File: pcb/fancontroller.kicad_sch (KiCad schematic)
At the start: 6 parts, among them J1 Thermo

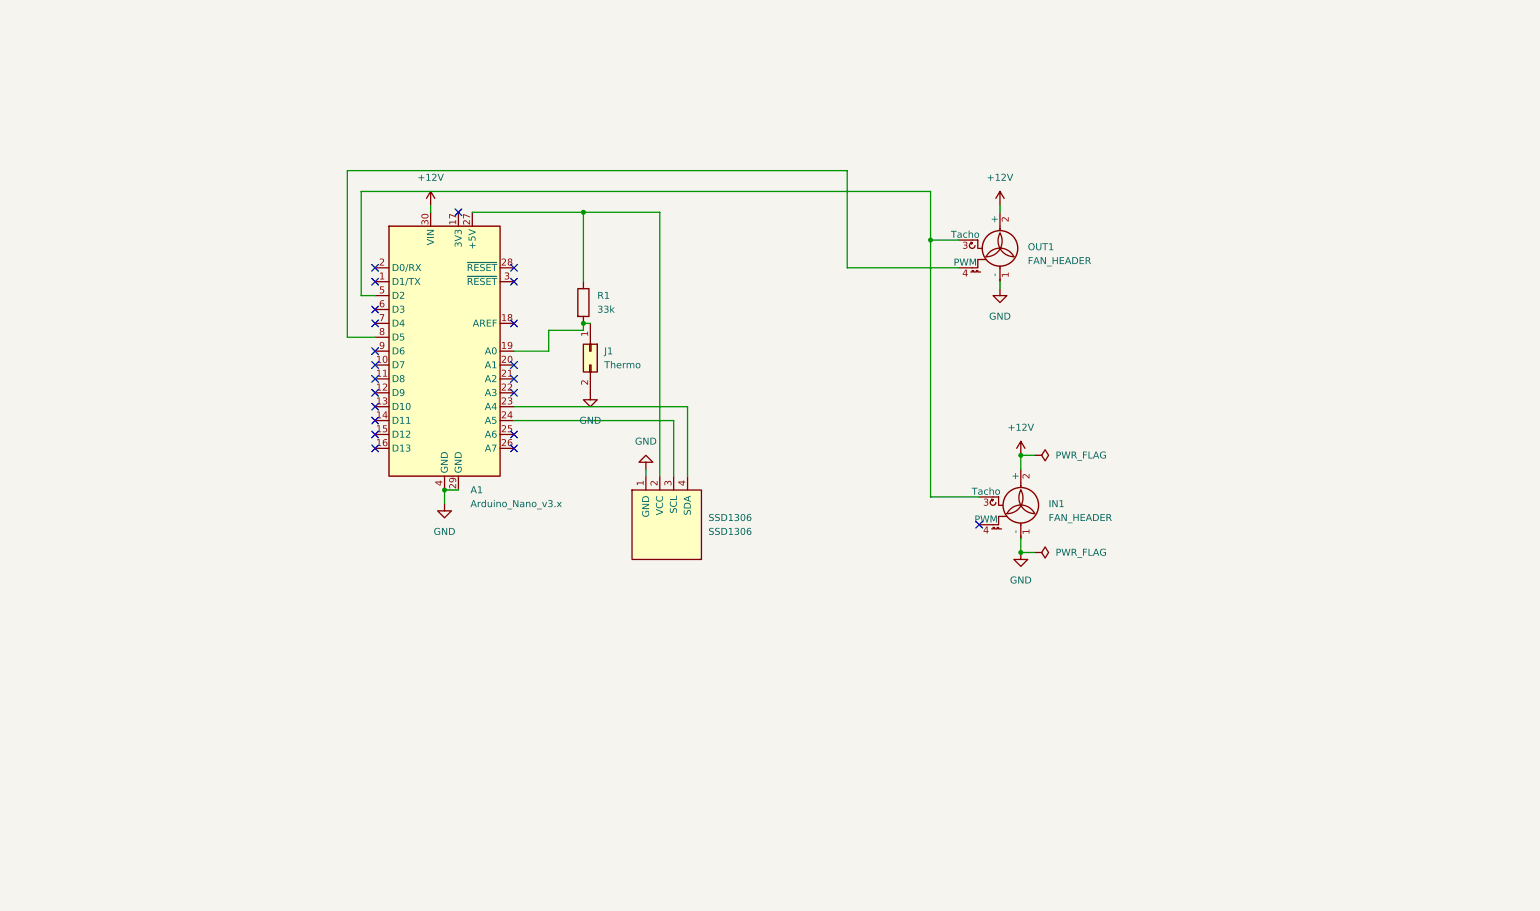
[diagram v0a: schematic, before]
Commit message: Update to Kicad 8, clean up schematic, add second fan header to schematic
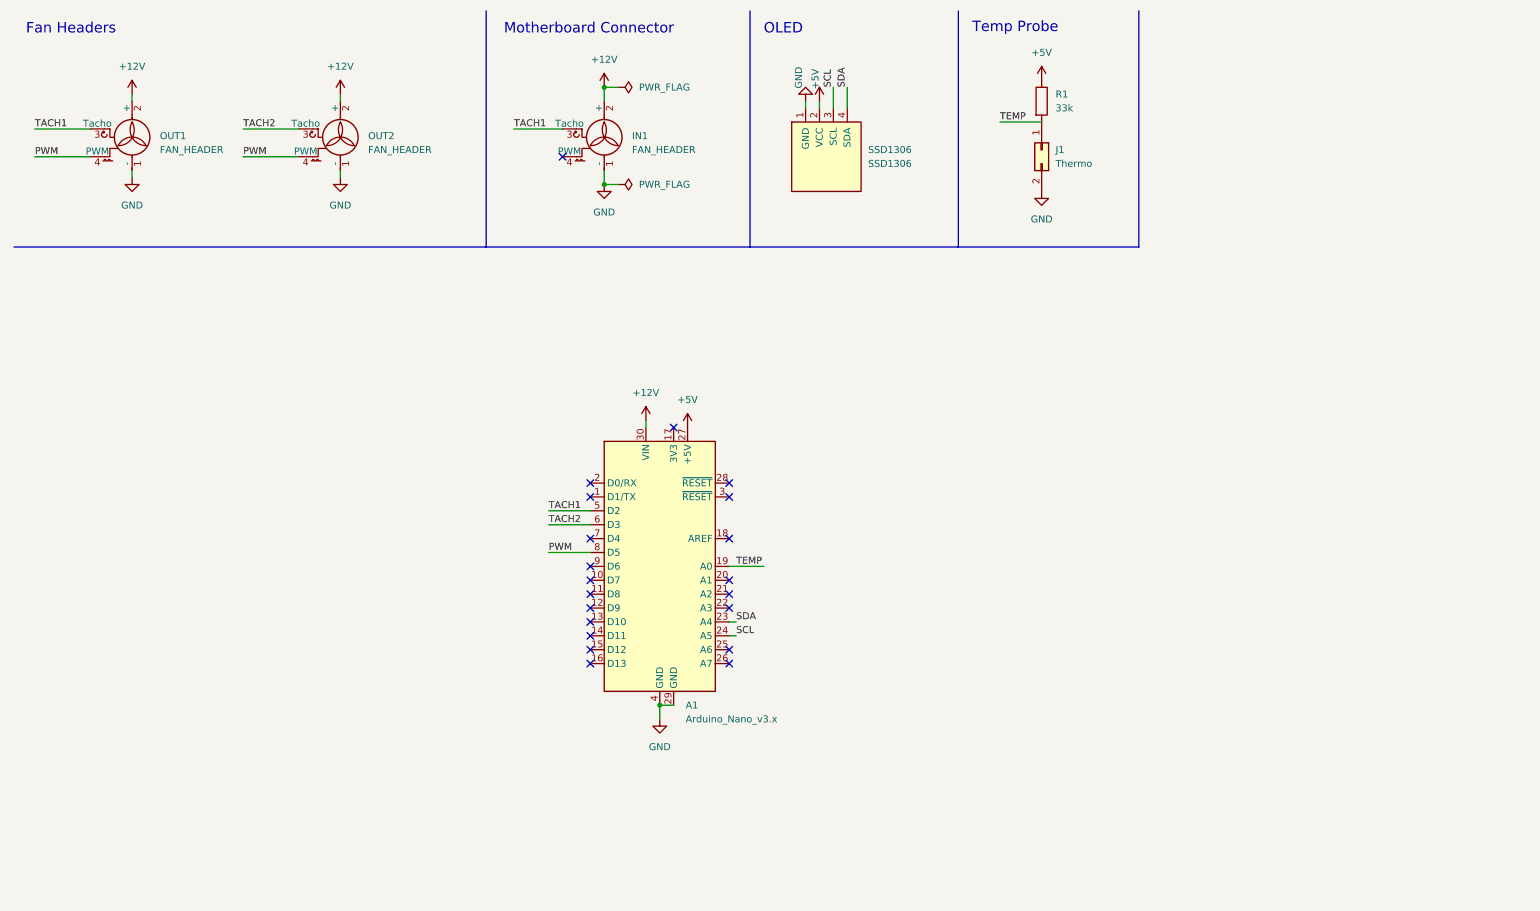
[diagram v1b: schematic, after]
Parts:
- added OUT2: FAN_HEADER, Connector:FanPinHeader_1x04_P2.54mm_Vertical, symbol Motor:Fan_CPU_4pin
- SSD1306: symbol SSD1306:SSD1306 -> SSD1306-128x64_OLED:SSD1306
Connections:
- net +12V: now also OUT2.2 (+)
- net GND: now also OUT2.1 (-)
- net TEMP: now reaches A1.19 (A0), J1.1 (Pin_1), R1.2
- net SDA: now reaches A1.23 (A4), SSD1306.4 (SDA)
- net SCL: now reaches A1.24 (A5), SSD1306.3 (SCL)
- net +5V: now reaches A1.27 (+5V), R1.1, SSD1306.2 (VCC)
- net TACH1: now reaches A1.5 (D2), IN1.3 (Tacho), OUT1.3 (Tacho)
- net TACH2: now reaches A1.6 (D3)
- net TACH2: now also OUT2.3 (Tacho)
- net PWM: now reaches A1.8 (D5), OUT1.4 (PWM)
- net PWM: now also OUT2.4 (PWM)
- no-connect marks 22 -> 21
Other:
- note added: "Fan Headers"
- note added: "Motherboard Connector"
- note added: "OLED"
- note added: "Temp Probe"
- company: (none) -> @funrollloops
- title: (none) -> Fan Controller
- moved on the sheet: A1, IN1, J1, OUT1, R1, SSD1306

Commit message: wip: switch to stm32f103
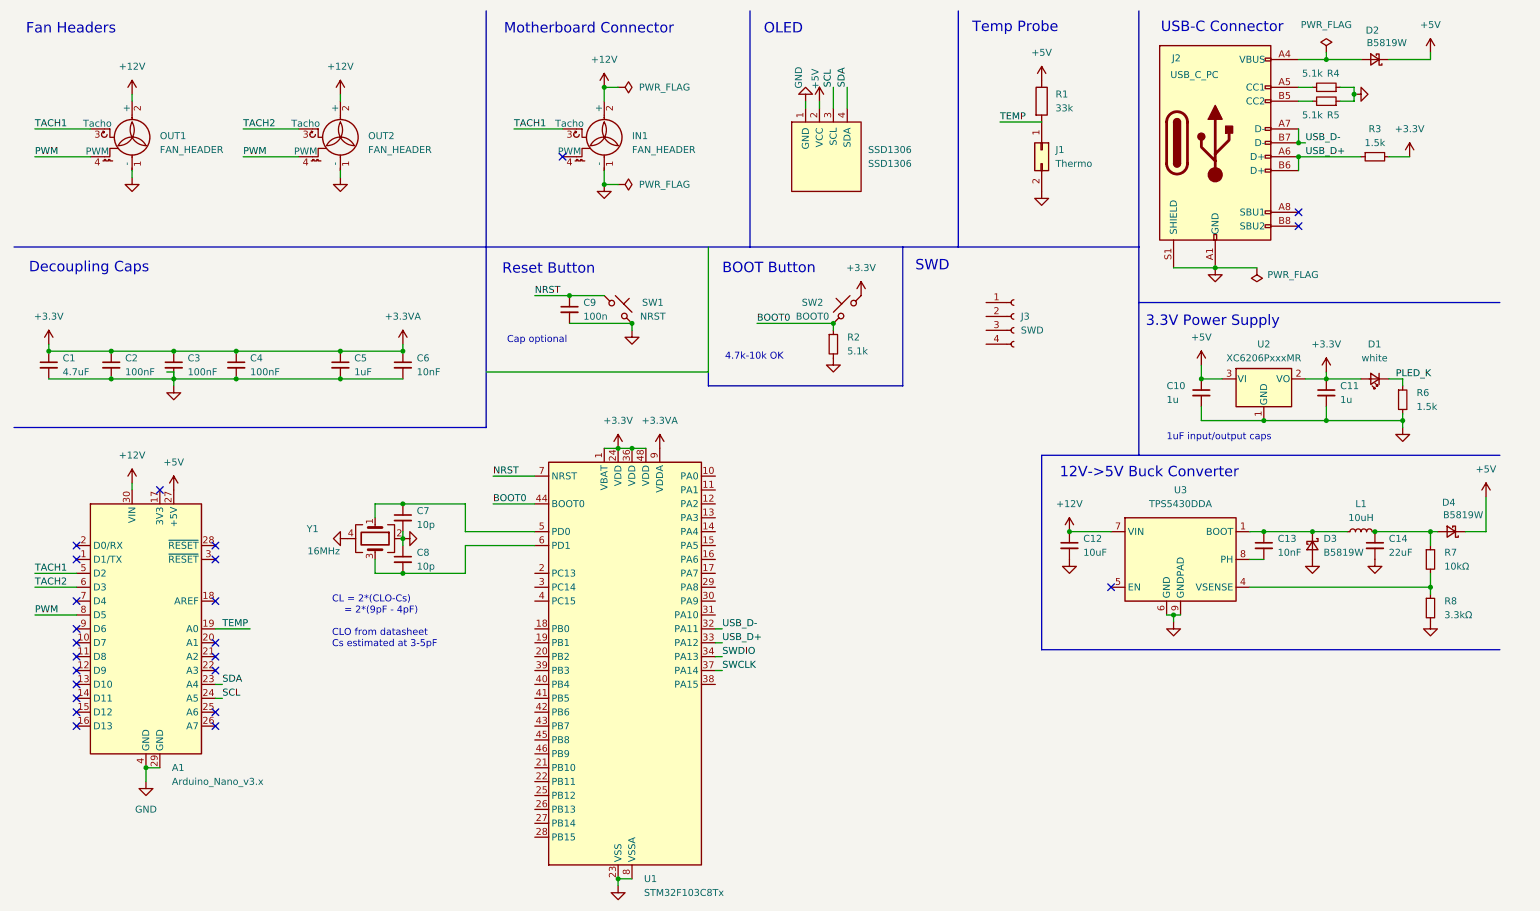
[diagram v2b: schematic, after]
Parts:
- added C1: 4.7uF, symbol Device:C_Small
- added C10, C11: 1u, Capacitor_SMD:C_0402_1005Metric, symbol Device:C_Small
- added C12: 10uF, symbol Device:C_Small
- added C13, C6: 10nF, symbol Device:C_Small
- added C14: 22uF, symbol Device:C_Small
- added C2, C3, C4: 100nF, symbol Device:C_Small
- added C5: 1uF, symbol Device:C_Small
- added C7, C8: 10p, Capacitor_SMD:C_0402_1005Metric, symbol Device:C_Small
- added C9: 100n, Capacitor_SMD:C_0402_1005Metric, symbol Device:C_Small
- added D1: white, LED_SMD:LED_0603_1608Metric, symbol Device:LED_Small
- added D2, D3, D4: B5819W, Diode_SMD:D_SOD-123, symbol Device:D_Schottky_Small
- added J2: USB_C_PC, Connector_USB:USB_C_Receptacle_XKB_U262-16XN-4BVC11, symbol Connector:USB_C_Receptacle_USB2.0_16P
- added J3: SWD, Connector_PinSocket_2.54mm:PinSocket_1x04_P2.54mm_Vertical, symbol Connector:Conn_01x04_Socket
- added L1: 10uH, symbol Device:L_Small
- added R2, R4, R5: 5.1k, Resistor_SMD:R_0402_1005Metric, symbol Device:R_Small
- added R3, R6: 1.5k, Resistor_SMD:R_0402_1005Metric, symbol Device:R_Small
- added R7: 10kΩ, symbol Device:R_Small
- added R8: 3.3kΩ, symbol Device:R_Small
- added SW1: NRST, Button_Switch_SMD:SW_Push_1P1T_XKB_TS-1187A, symbol Switch:SW_Push_45deg
- added SW2: BOOT0, Button_Switch_SMD:SW_Push_1P1T_XKB_TS-1187A, symbol Switch:SW_Push_45deg
- added U1: STM32F103C8Tx, Package_QFP:LQFP-48_7x7mm_P0.5mm, symbol MCU_ST_STM32F1:STM32F103C8Tx
- added U2: XC6206PxxxMR, Package_TO_SOT_SMD:SOT-23-3, symbol Regulator_Linear:XC6206PxxxMR
- added U3: TPS5430DDA, Package_SO:TI_SO-PowerPAD-8_ThermalVias, symbol Regulator_Switching:TPS5430DDA
- added Y1: 16MHz, Crystal:Crystal_SMD_3225-4Pin_3.2x2.5mm, symbol Device:Crystal_GND24
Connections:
- net +12V: now also C12.1, U3.7 (VIN)
- net +5V: now also C10.1, D2.1 (K), D4.1 (K), U2.3 (VI)
- net GND: now also C1.2, C10.2, C11.2, C12.2, C14.2, C2.2, C3.2, C4.2, C5.2, C6.2, C7.2, C8.1, C9.2, D3.2 (A), J2.A1 (GND), J2.A12 (GND), J2.B1 (GND), J2.B12 (GND), J2.S1 (SHIELD), R2.2, R4.1, R5.1, R6.2, R8.2, SW1.2, U1.23 (VSS), U1.35 (VSS), U1.47 (VSS), U1.8 (VSSA), U2.1 (GND), U3.6 (GND), U3.9 (GNDPAD), Y1.2, Y1.4
- new net: C13.1, D3.1 (K), L1.1, U3.1 (BOOT)
- new net: C13.2, U3.8 (PH)
- new net: D2.2 (A), J2.A4 (VBUS), J2.A9 (VBUS), J2.B4 (VBUS), J2.B9 (VBUS)
- new net: J2.A5 (CC1), R4.2
- new net: J2.B5 (CC2), R5.2
- new net: C14.1, D4.2 (A), L1.2, R7.1
- new net: C7.1, U1.5 (PD0), Y1.1
- new net: C8.2, U1.6 (PD1), Y1.3
- new net: R7.2, R8.1, U3.4 (VSENSE)
- new net +3.3V: C1.1, C11.1, C2.1, C3.1, C4.1, C5.1, C6.1, D1.2 (A), R3.2, SW2.1, U1.1 (VBAT), U1.24 (VDD), U1.36 (VDD), U1.48 (VDD), U1.9 (VDDA), U2.2 (VO)
- new net BOOT0: R2.1, SW2.2, U1.44 (BOOT0)
- new net NRST: C9.1, SW1.1, U1.7 (NRST)
- new net PLED_K: D1.1 (K), R6.1
- new net SWCLK: U1.37 (PA14)
- new net SWDIO: U1.34 (PA13)
- new net USB_D+: J2.A6 (D+), J2.B6 (D+), R3.1, U1.33 (PA12)
- new net USB_D-: J2.A7 (D-), J2.B7 (D-), U1.32 (PA11)
- no-connect marks 21 -> 24
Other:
- note added: "12V->5V Buck Converter"
- note added: "1uF input/output caps"
- note added: "3.3V Power Supply"
- note added: "4.7k-10k OK"
- note added: "BOOT Button"
- note added: "CL = 2*(CLO-Cs) = 2*(9pF - 4pF) CLO from datasheet Cs estimated at 3-5pF"
- note added: "Cap optional"
- note added: "Decoupling Caps"
- note added: "Reset Button"
- note added: "SWD"
- note added: "USB-C Connector"
- moved on the sheet: A1

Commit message: v2: add stm32cubemx config, early draft of pcb layout, update version
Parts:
- removed A1: Arduino_Nano_v3.x, Module:Arduino_Nano, symbol MCU_Module:Arduino_Nano_v3.x
- added U4: USBLC6-2SC6, Package_TO_SOT_SMD:SOT-23-6, symbol Power_Protection:USBLC6-2SC6
- C1, C13, C2, C3, C4, C5, C6: footprint (none) -> Capacitor_SMD:C_0402_1005Metric
- C10, C11: value 1u -> 1uF
- C12, C14: footprint (none) -> Capacitor_SMD:C_0603_1608Metric
- C7, C8: value 10p -> 10pF
- L1: footprint (none) -> Inductor_SMD:L_1210_3225Metric
- R1: value 33k -> 33kΩ; footprint Resistor_THT:R_Axial_DIN0207_L6.3mm_D2.5mm_P7.62mm_Horizontal -> Resistor_SMD:R_0402_1005Metric
- R2, R4, R5: value 5.1k -> 5.1kΩ
- R3, R6: value 1.5k -> 1.5kΩ
- R7, R8: footprint (none) -> Resistor_SMD:R_0402_1005Metric
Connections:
- net +3.3V: now also J3.4 (Pin_4), R1.1, SSD1306.2 (VCC)
- net +5V: no longer R1.1, SSD1306.2 (VCC)
- net GND: now also J3.1 (Pin_1), U4.2 (GND)
- net PWM: now also U1.28 (PB15)
- net SCL: now also U1.42 (PB6)
- net SDA: now also U1.43 (PB7)
- net SWCLK: now also J3.2 (Pin_2)
- net SWDIO: now also J3.3 (Pin_3)
- net TACH1: now also U1.25 (PB12)
- net TACH2: now also U1.26 (PB13)
- net TEMP: now also U1.11 (PA1)
- net USB_D+: now also U4.1 (I/O1), U4.6 (I/O1)
- net USB_D-: now also U4.3 (I/O2), U4.4 (I/O2)
- net at C13.1, U3.1 (BOOT): no longer D3.1 (K), L1.1
- net at C13.2, U3.8 (PH): now also D3.1 (K), L1.1
- net VBUS: now reaches D2.2 (A), J2.A4 (VBUS), J2.A9 (VBUS), J2.B4 (VBUS), J2.B9 (VBUS)
- net VBUS: now also U4.5 (VBUS)
- no-connect marks 24 -> 29
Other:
- note added: "5V -> 3.3V LDO"
- note removed: "3.3V Power Supply"
- title: Fan Controller -> Fan Controller (v2, WIP)
- moved on the sheet: D2, J3, L1, R3

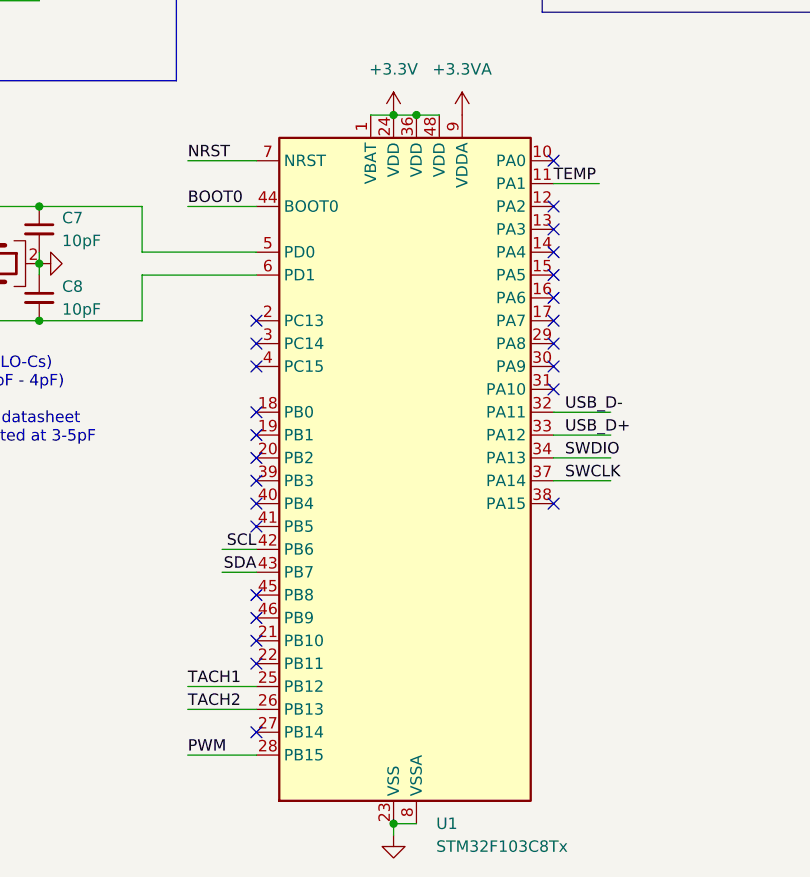
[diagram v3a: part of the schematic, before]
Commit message: Finish routing assuming OLED module
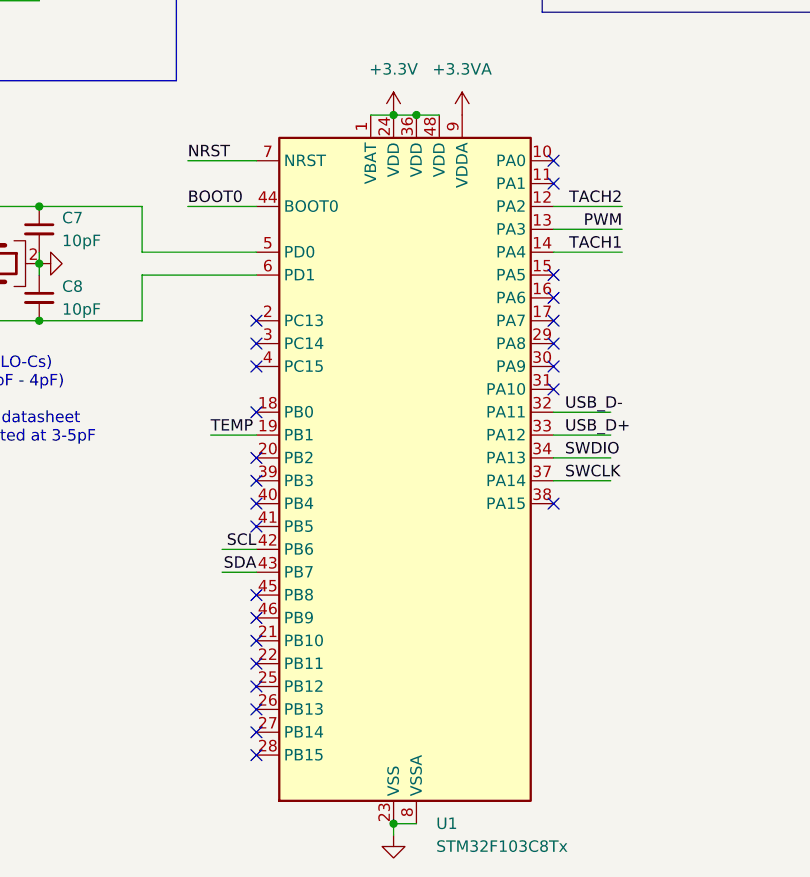
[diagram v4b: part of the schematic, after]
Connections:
- net PWM: now also U1.13 (PA3); no longer U1.28 (PB15)
- net TACH1: now also U1.14 (PA4); no longer U1.25 (PB12)
- net TACH2: now also U1.12 (PA2); no longer U1.26 (PB13)
- net TEMP: now also U1.19 (PB1); no longer U1.11 (PA1)
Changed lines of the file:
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@@
+	)
+	(no_connect
+		(at 107.95 158.75)
+	)
+	(no_connect
+		(at 107.95 156.21)
 	)
 	(no_connect
@@
 	)
 	(no_connect
-		(at 140.97 102.87)
-	)
-	(no_connect
 		(at 107.95 125.73)
 	)
@@
 	)
 	(no_connect
+		(at 107.95 163.83)
+	)
+	(no_connect
 		(at 107.95 133.35)
 	)
@@
 	)
 	(no_connect
-		(at 140.97 107.95)
+		(at 140.97 100.33)
 	)
 	(no_connect
@@
 	)
 	(no_connect
-		(at 140.97 105.41)
-	)
-	(no_connect
 		(at 140.97 97.79)
 	)
@@
 	)
 	(no_connect
-		(at 107.95 128.27)
-	)
-	(no_connect
 		(at 140.97 118.11)
 	)
@@
 	(wire
 		(pts
-			(xy 100.33 158.75) (xy 107.95 158.75)
+			(xy 148.59 102.87) (xy 140.97 102.87)
 		)
 		(stroke
@@
 	(wire
 		(pts
-			(xy 140.97 100.33) (xy 146.05 100.33)
+			(xy 102.87 128.27) (xy 107.95 128.27)
 		)
 		(stroke
@@
 	(wire
 		(pts
-			(xy 100.33 156.21) (xy 107.95 156.21)
+			(xy 148.59 107.95) (xy 140.97 107.95)
 		)
 		(stroke
@@
 	(wire
 		(pts
-			(xy 100.33 163.83) (xy 107.95 163.83)
+			(xy 148.59 105.41) (xy 140.97 105.41)
 		)
 		(stroke
@@
 	)
 	(label "TACH1"
-		(at 100.33 156.21 0)
-		(fields_autoplaced yes)
-		(effects
-			(font
-				(size 1.27 1.27)
-			)
-			(justify left bottom)
+		(at 148.59 107.95 180)
+		(fields_autoplaced yes)
+		(effects
+			(font
+				(size 1.27 1.27)
+			)
+			(justify right bottom)
 		)
 	)
@@
 	)
 	(label "TEMP"
-		(at 140.97 100.33 0)
+		(at 102.87 128.27 0)
 		(fields_autoplaced yes)
 		(effects
@@
 	)
 	(label "PWM"
-		(at 100.33 163.83 0)
-		(fields_autoplaced yes)
-		(effects
-			(font
-				(size 1.27 1.27)
-			)
-			(justify left bottom)
+		(at 148.59 105.41 180)
+		(fields_autoplaced yes)
+		(effects
+			(font
+				(size 1.27 1.27)
+			)
+			(justify right bottom)
 		)
 	)
@@
 	)
 	(label "TACH2"
-		(at 100.33 158.75 0)
-		(fields_autoplaced yes)
-		(effects
-			(font
-				(size 1.27 1.27)
-			)
-			(justify left bottom)
-		)
-	)
+		(at 148.59 102.87 180)
+		(fields_autoplaced yes)
+		(effects
+			(font
+				(size 1.27 1.27)
+			)
+			(justify right bottom)
+		)
+	)
